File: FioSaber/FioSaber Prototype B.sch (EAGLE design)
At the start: 19 parts, among them P1 WIICHUCK, T1 2N2222

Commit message: prototype b
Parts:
- removed I2C: 1X4-BIG, adafruit:1X4-BIG
- removed LED1, LED2, LED3, LED4: (no value), adafruit:LED3MM
- removed R5: 33Ω, adafruit:R-US_0207/10
- removed R6: 1kΩ, adafruit:R-US_0207/10
- removed U$1: 1X2, headers(.1in):1X2
- added D2: 1N4004, adafruit:1N4004
- added IN, OUT: (no value), adafruit:JST_2PIN-SMT-RA
- added MODE: 5MMRGBLED, adafruit:5MMRGBLED
- added S1: (no value), adafruit:EG1218S
- added TX: (no value), adafruit:LED3MM
- R3: value 100Ω -> 1kΩ
- R4: value 100Ω -> 33Ω
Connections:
- removed net N$14: FIOR.4, U$1.2
- removed net N$15: FIOR.5, U$1.1
- new net N$25: R2.2, TX.A
- net N$1: no longer I2C.2
- net N$10: now also OUT.2, S1.P; no longer LED2.A, R2.2
- net N$11: now also IN.1, OUT.1; no longer LED3.A, R3.2
- net N$12: now also FIOR.3, R4.1; no longer LED4.A, R4.2
- net N$13: now also MODE.GND, R1.2, T1.E; no longer FIOL.2, I2C.1, LED1.C, LED2.C, LED3.C, LED4.C, P1.GND
- net N$16: now also R3.2; no longer R6.2
- net N$17: now also FIOR.12, R2.1; no longer FIOR.1, T1.E
- net N$18: now also R3.1; no longer R6.1
- net N$19: now also D2.A; no longer D1.A
- net N$2: now also D1.C, IN.2, S1.S; no longer FIOR.3, R5.1
- net N$20: now also D2.C, R4.2; no longer D1.C, R5.2
- net N$3: no longer I2C.3
- net N$4: no longer I2C.4
- net N$5: now also D1.A, S1.O; no longer FIOR.12, R1.1
- net N$6: now also MODE.BLUE; no longer R2.1
- net N$7: now also MODE.GREEN; no longer R3.1
- net N$8: now also MODE.RED; no longer R4.1
- net N$9: now also FIOL.2, P1.GND, R1.1, TX.C; no longer LED1.A, R1.2
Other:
- moved on the sheet: C1, D1, FIOL, P1, R1, R2, R3, R4, T1

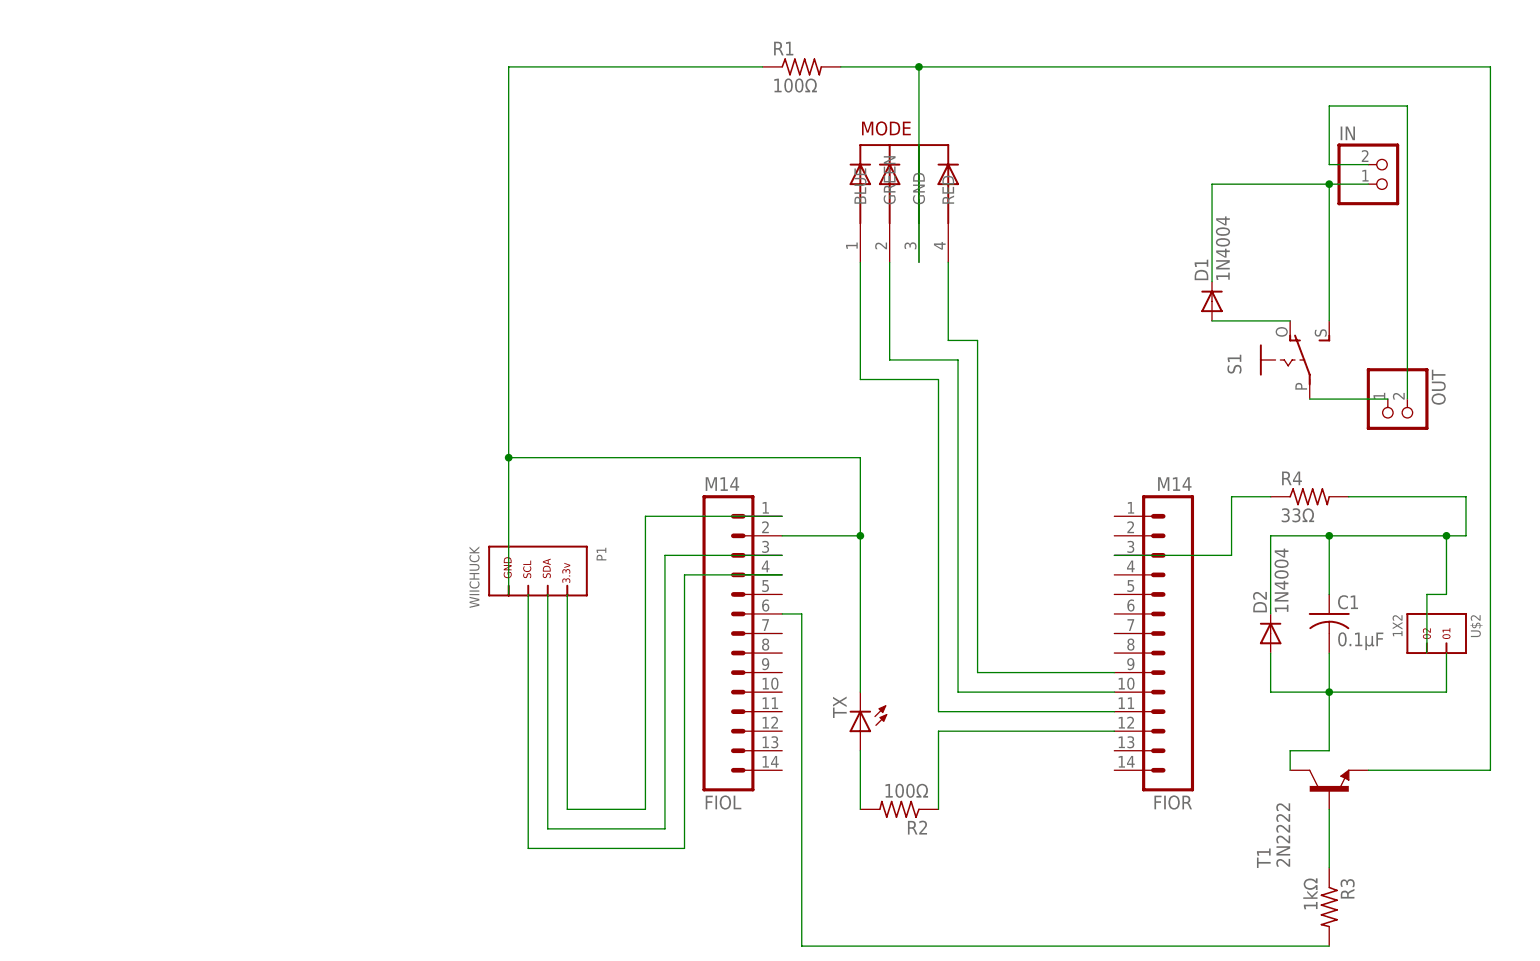
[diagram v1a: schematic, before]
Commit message: added manual mode switch
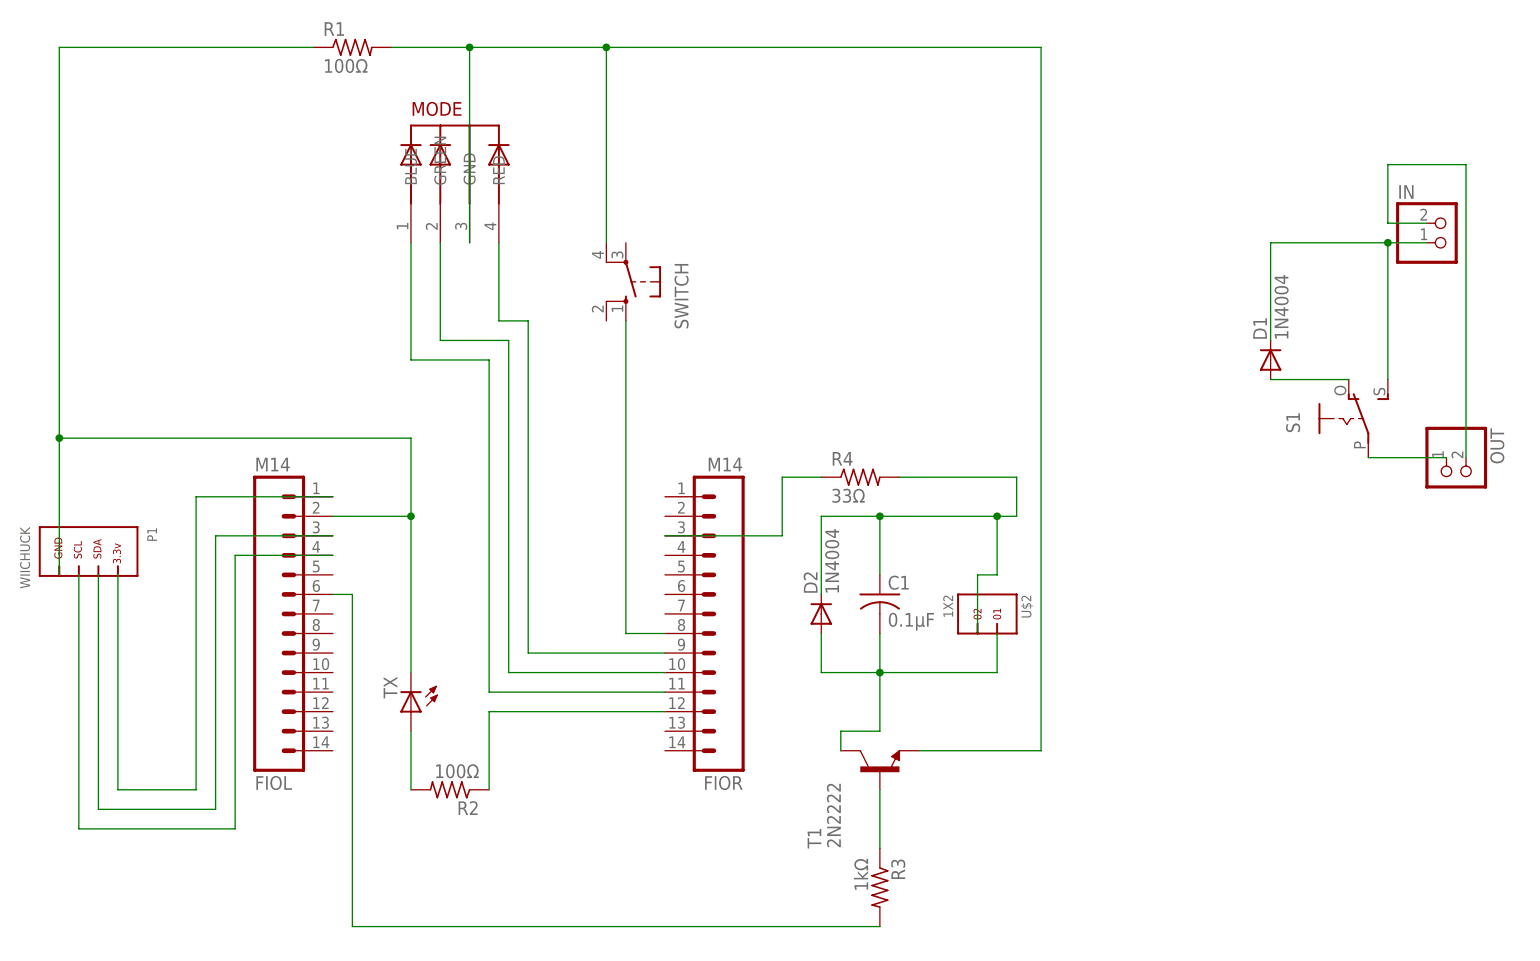
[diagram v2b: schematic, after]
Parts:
- added SWITCH: (no value), switch-omron:10-XX
- R1, R2, R3, R4: device adafruit:R-US_0207/10 -> adafruit:R-US_0207/7
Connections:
- new net N$14: FIOR.8, SWITCH.S
- net N$13: now also SWITCH.P1
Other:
- moved on the sheet: C1, D1, D2, FIOL, FIOR, IN, MODE, OUT, P1, R1, R2, R3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

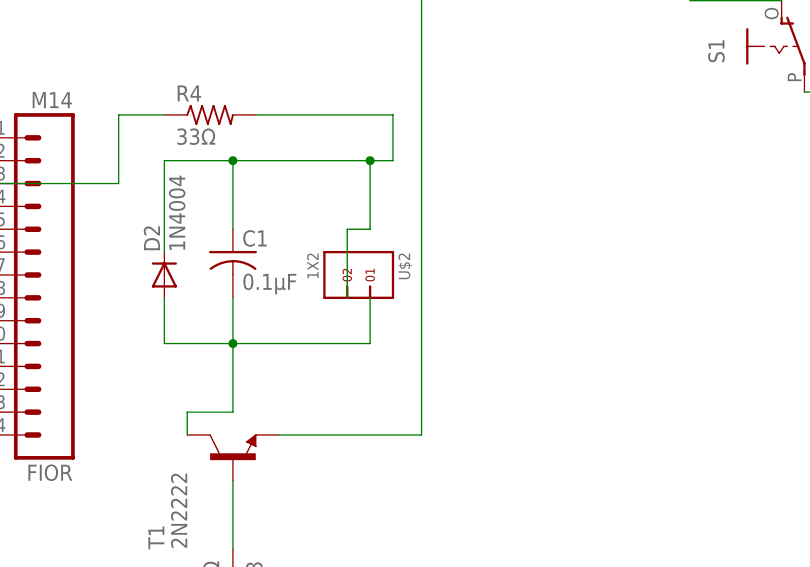
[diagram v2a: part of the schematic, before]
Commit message: labeled motor header
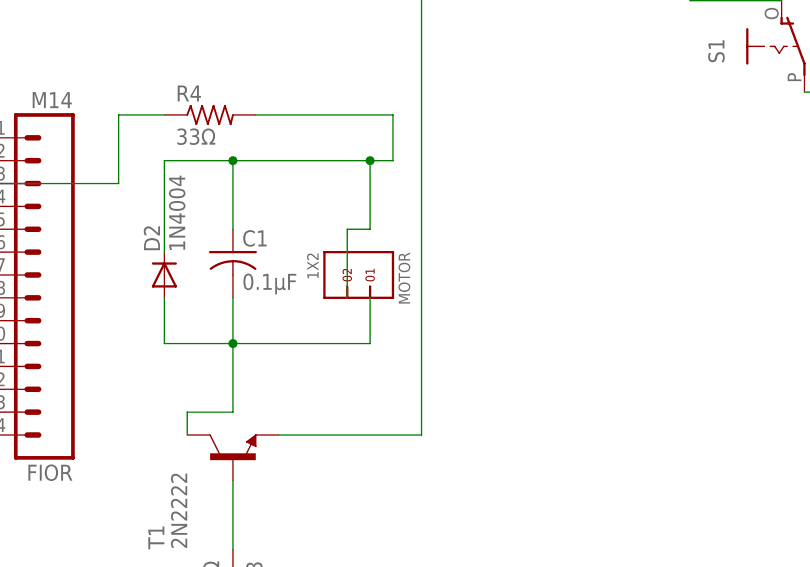
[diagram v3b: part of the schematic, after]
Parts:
- renumbered U$2 to MOTOR
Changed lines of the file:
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@@
 <part name="R4" library="adafruit" deviceset="R-US_" device="0207/7" value="33Ω"/>
 <part name="R3" library="adafruit" deviceset="R-US_" device="0207/7" value="1kΩ"/>
-<part name="U$2" library="headers(.1in)" deviceset="1X2" device=""/>
+<part name="MOTOR" library="headers(.1in)" deviceset="1X2" device=""/>
 <part name="D1" library="adafruit" deviceset="1N4004" device=""/>
 <part name="S1" library="adafruit" deviceset="EG1218" device="S"/>
@@
 <instance part="R4" gate="G$1" x="127" y="111.76"/>
 <instance part="R3" gate="G$1" x="129.54" y="58.42" rot="R270"/>
-<instance part="U$2" gate="G$1" x="144.78" y="93.98" rot="R270"/>
+<instance part="MOTOR" gate="G$1" x="144.78" y="93.98" rot="R270"/>
 <instance part="D1" gate="1" x="180.34" y="127" rot="R90"/>
 <instance part="S1" gate="1" x="190.5" y="119.38"/>
@@
 <wire x1="129.54" y1="86.36" x2="121.92" y2="86.36" width="0.1524" layer="91"/>
 <wire x1="129.54" y1="86.36" x2="144.78" y2="86.36" width="0.1524" layer="91"/>
-<pinref part="U$2" gate="G$1" pin="1"/>
+<pinref part="MOTOR" gate="G$1" pin="1"/>
 <wire x1="144.78" y1="86.36" x2="144.78" y2="91.44" width="0.1524" layer="91"/>
 <junction x="129.54" y="86.36"/>
@@
 <net name="N$20" class="0">
 <segment>
-<pinref part="U$2" gate="G$1" pin="2"/>
+<pinref part="MOTOR" gate="G$1" pin="2"/>
 <wire x1="121.92" y1="106.68" x2="129.54" y2="106.68" width="0.1524" layer="91"/>
 <wire x1="129.54" y1="106.68" x2="144.78" y2="106.68" width="0.1524" layer="91"/>

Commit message: reconfigured prototype b
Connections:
- removed net N$12: FIOR.3, R4.1
- net N$9: now also R4.1
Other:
- moved on the sheet: R4
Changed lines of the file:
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@@
 <instance part="T1" gate="G$1" x="129.54" y="73.66" rot="R90"/>
 <instance part="C1" gate="G$1" x="129.54" y="96.52"/>
-<instance part="R4" gate="G$1" x="127" y="111.76"/>
+<instance part="R4" gate="G$1" x="127" y="116.84"/>
 <instance part="R3" gate="G$1" x="129.54" y="58.42" rot="R270"/>
 <instance part="MOTOR" gate="G$1" x="144.78" y="93.98" rot="R270"/>
@@
 <wire x1="142.24" y1="99.06" x2="142.24" y2="91.44" width="0.1524" layer="91"/>
 <pinref part="R4" gate="G$1" pin="2"/>
-<wire x1="132.08" y1="111.76" x2="147.32" y2="111.76" width="0.1524" layer="91"/>
-<wire x1="147.32" y1="111.76" x2="147.32" y2="106.68" width="0.1524" layer="91"/>
+<wire x1="132.08" y1="116.84" x2="147.32" y2="116.84" width="0.1524" layer="91"/>
+<wire x1="147.32" y1="116.84" x2="147.32" y2="106.68" width="0.1524" layer="91"/>
 <wire x1="147.32" y1="106.68" x2="144.78" y2="106.68" width="0.1524" layer="91"/>
 <junction x="144.78" y="106.68"/>
@@
 <wire x1="205.74" y1="152.4" x2="205.74" y2="114.3" width="0.1524" layer="91"/>
 <pinref part="OUT" gate="G$1" pin="1"/>
-</segment>
-</net>
-<net name="N$12" class="0">
-<segment>
-<pinref part="R4" gate="G$1" pin="1"/>
-<wire x1="121.92" y1="111.76" x2="116.84" y2="111.76" width="0.1524" layer="91"/>
-<wire x1="116.84" y1="111.76" x2="116.84" y2="104.14" width="0.1524" layer="91"/>
-<pinref part="FIOR" gate="G$1" pin="3"/>
-<wire x1="116.84" y1="104.14" x2="101.6" y2="104.14" width="0.1524" layer="91"/>
 </segment>
 </net>
@@
 <junction x="22.86" y="116.84"/>
 <junction x="68.58" y="106.68"/>
-</segment>
-</net>
+<pinref part="R4" gate="G$1" pin="1"/>
+<wire x1="68.58" y1="116.84" x2="121.92" y2="116.84" width="0.1524" layer="91"/>
+<junction x="68.58" y="116.84"/>
+</segment>
+</net>

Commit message: prototype b tweaks
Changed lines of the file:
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@@
 <pinref part="T1" gate="G$1" pin="E"/>
 <wire x1="76.2" y1="167.64" x2="93.98" y2="167.64" width="0.1524" layer="91"/>
-<wire x1="93.98" y1="167.64" x2="150.495" y2="167.64" width="0.1524" layer="91"/>
-<wire x1="150.495" y1="167.64" x2="150.495" y2="76.2" width="0.1524" layer="91"/>
-<wire x1="150.495" y1="76.2" x2="134.62" y2="76.2" width="0.1524" layer="91"/>
+<wire x1="93.98" y1="167.64" x2="155.575" y2="167.64" width="0.1524" layer="91"/>
+<wire x1="155.575" y1="167.64" x2="155.575" y2="76.2" width="0.1524" layer="91"/>
+<wire x1="155.575" y1="76.2" x2="134.62" y2="76.2" width="0.1524" layer="91"/>
 <pinref part="MODE" gate="G$1" pin="GND"/>
 <wire x1="76.2" y1="142.24" x2="76.2" y2="167.64" width="0.1524" layer="91"/>
